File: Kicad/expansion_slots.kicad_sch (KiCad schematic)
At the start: 32 parts, among them J901 Conn_01x06, J902 Neotron-Expansion-Slot, J903 Neotron-Expansion-Slot, J904 Neotron-Expansion-Slot, J905 Neotron-Expansion-Slot, J906 Conn_01x09, J907 Conn_01x09, J908 Conn_01x09

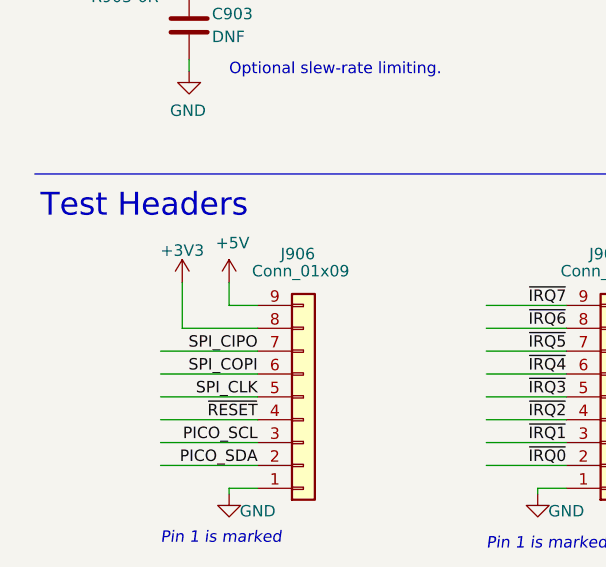
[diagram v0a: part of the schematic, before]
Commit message: Updated to KiCAD 7.
Had to move a net-tie to resolve a "too close" error.
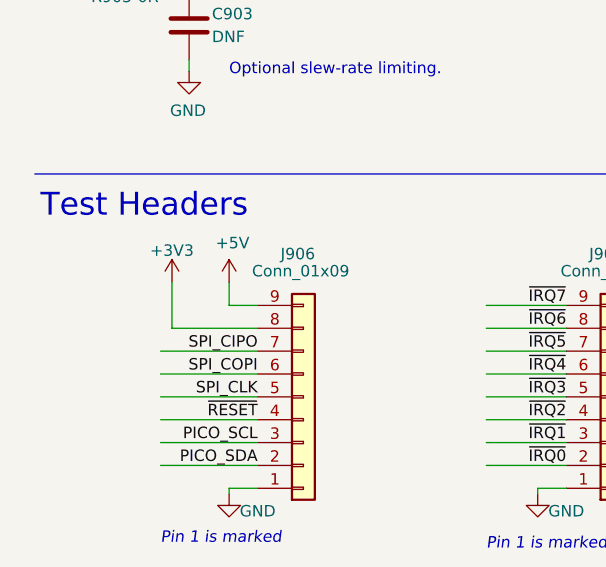
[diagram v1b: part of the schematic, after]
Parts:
- J901: symbol Connector:Conn_01x06_Male -> Connector:Conn_01x06_Pin
